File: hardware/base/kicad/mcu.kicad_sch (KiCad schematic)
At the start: 37 parts, among them J2 USB micro-B, J5 TC2030, SW1 BOOT, U2 TPD4E05U06DQAR, U9 STM32H523VET6

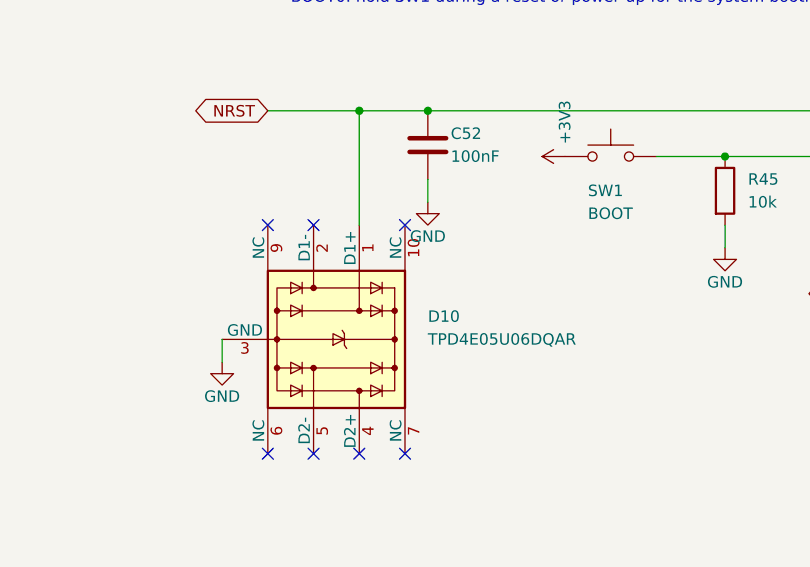
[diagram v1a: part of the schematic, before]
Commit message: Flow-through ESD arrays: the NC pin opposite each protected line carries it on every TPD4E05, not only on the PHY lines
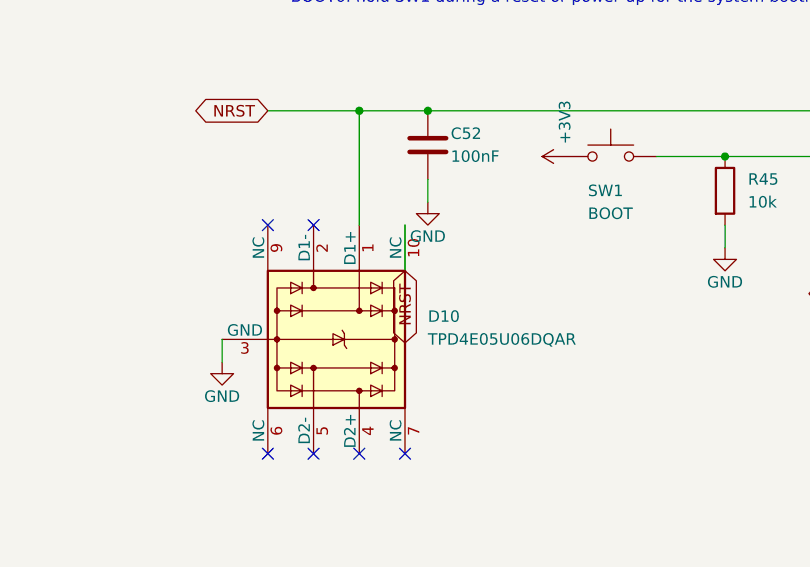
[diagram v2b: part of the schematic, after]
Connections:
- net NRST: now also D10.10 (NC)
- no-connect marks 10 -> 9

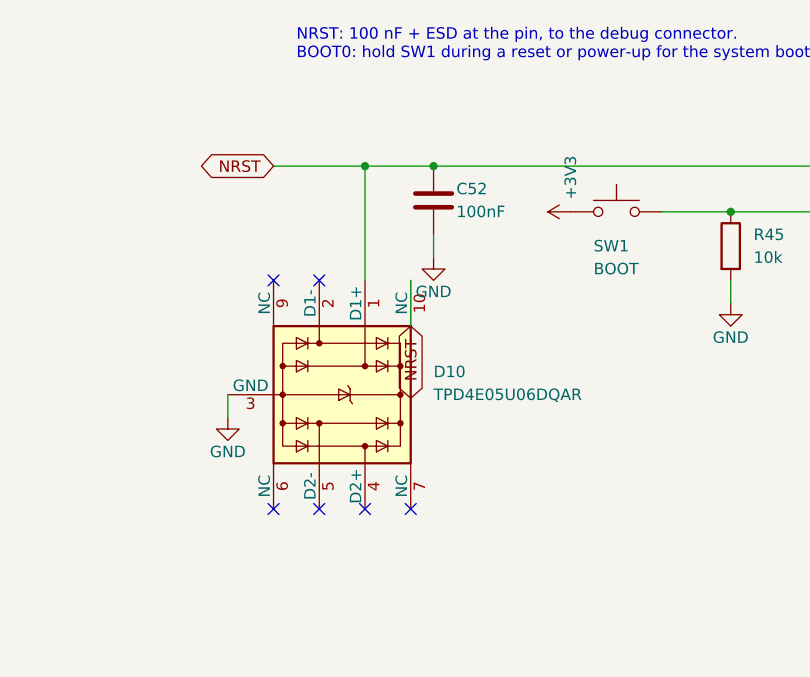
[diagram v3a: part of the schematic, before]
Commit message: Modbus termination always fitted (R246, removed for a master in the middle of the line); no ESD array on NRST; Ethernet line nets named TXA_P/TXA_N so that tools pair them
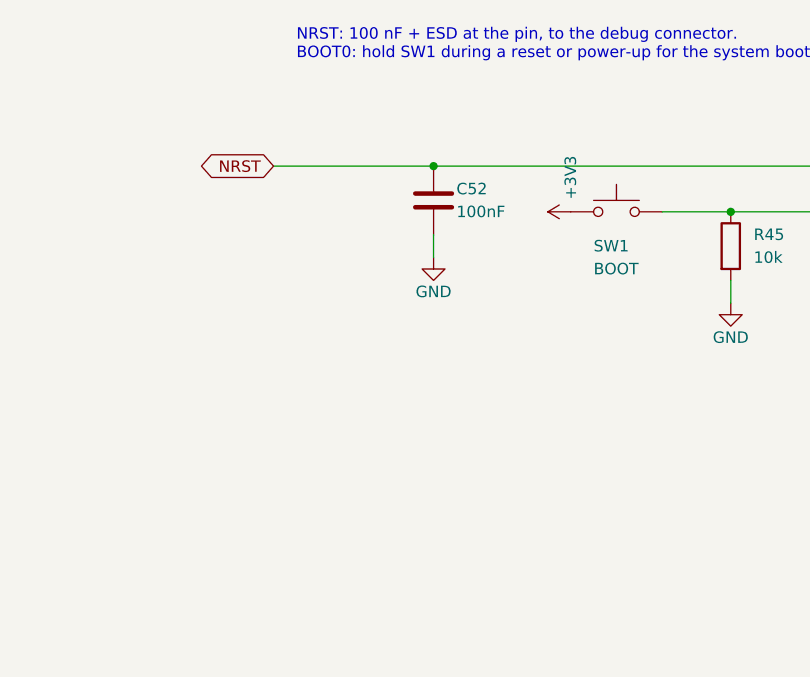
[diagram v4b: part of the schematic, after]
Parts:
- removed D10: TPD4E05U06DQAR, Package_SON:USON-10_2.5x1.0mm_P0.5mm, symbol Power_Protection:TPD4E05U06DQA
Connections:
- no-connect marks 9 -> 3

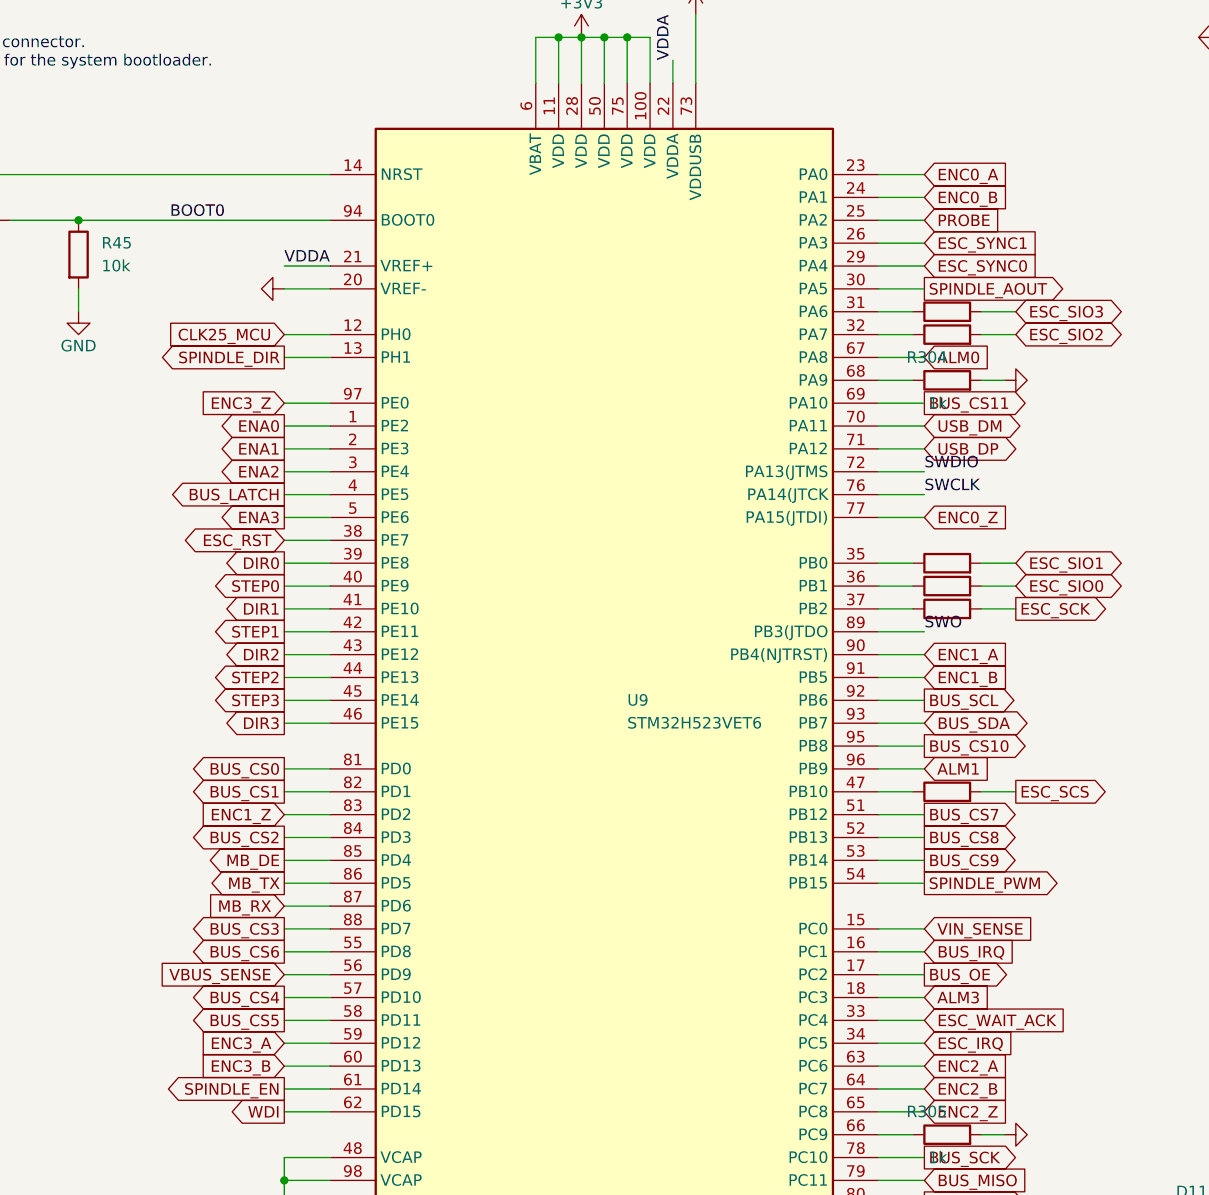
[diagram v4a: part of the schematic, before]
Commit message: Base: pin swaps of the placed board (chip selects, step/dir/enable channels, encoder timers 0 and 1, ribbon and Ethernet A ESD channels)
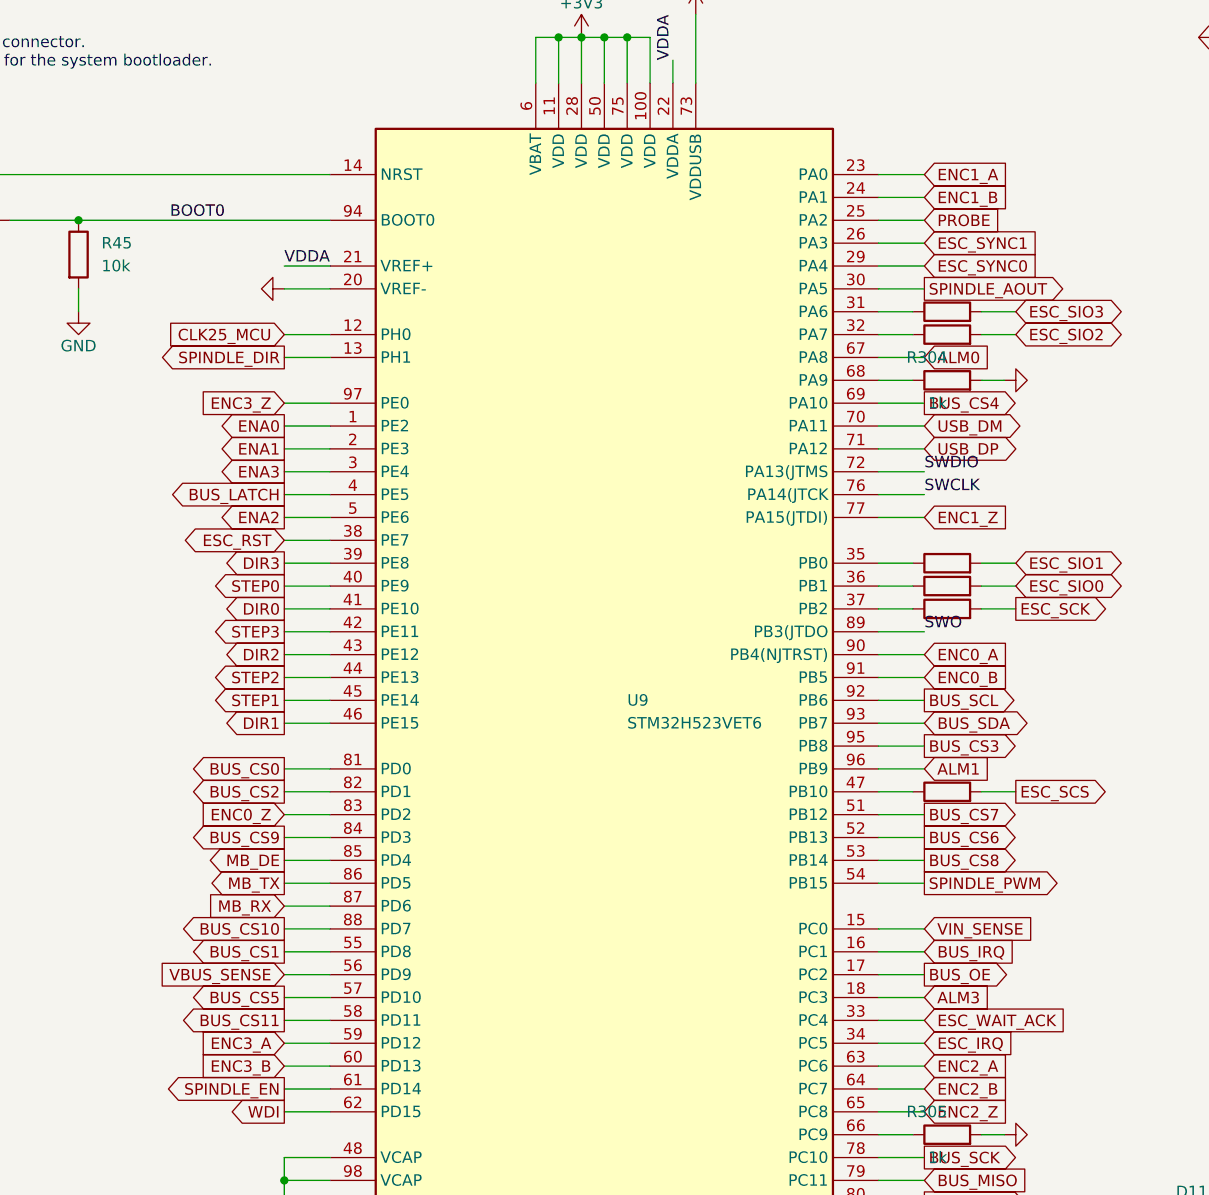
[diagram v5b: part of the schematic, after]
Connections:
- net BUS_CS1: now also U9.55 (PD8); no longer U9.82 (PD1)
- net BUS_CS10: now also U9.88 (PD7); no longer U9.95 (PB8)
- net BUS_CS11: now also U9.58 (PD11); no longer U9.69 (PA10)
- net BUS_CS2: now also U9.82 (PD1); no longer U9.84 (PD3)
- net BUS_CS3: now also U9.95 (PB8); no longer U9.88 (PD7)
- net BUS_CS4: now also U9.69 (PA10); no longer U9.57 (PD10)
- net BUS_CS5: now also U9.57 (PD10); no longer U9.58 (PD11)
- net BUS_CS6: now also U9.52 (PB13); no longer U9.55 (PD8)
- net BUS_CS8: now also U9.53 (PB14); no longer U9.52 (PB13)
- net BUS_CS9: now also U9.84 (PD3); no longer U9.53 (PB14)
- net DIR0: now also U9.41 (PE10); no longer U9.39 (PE8)
- net DIR1: now also U9.46 (PE15); no longer U9.41 (PE10)
- net DIR3: now also U9.39 (PE8); no longer U9.46 (PE15)
- net ENA2: now also U9.5 (PE6); no longer U9.3 (PE4)
- net ENA3: now also U9.3 (PE4); no longer U9.5 (PE6)
- net ENC0_A: now also U9.90 (PB4(NJTRST)); no longer U9.23 (PA0)
- net ENC0_B: now also U9.91 (PB5); no longer U9.24 (PA1)
- net ENC0_Z: now also U9.83 (PD2); no longer U9.77 (PA15(JTDI))
- net ENC1_A: now also U9.23 (PA0); no longer U9.90 (PB4(NJTRST))
- net ENC1_B: now also U9.24 (PA1); no longer U9.91 (PB5)
- net ENC1_Z: now also U9.77 (PA15(JTDI)); no longer U9.83 (PD2)
- net STEP1: now also U9.45 (PE14); no longer U9.42 (PE11)
- net STEP3: now also U9.42 (PE11); no longer U9.45 (PE14)

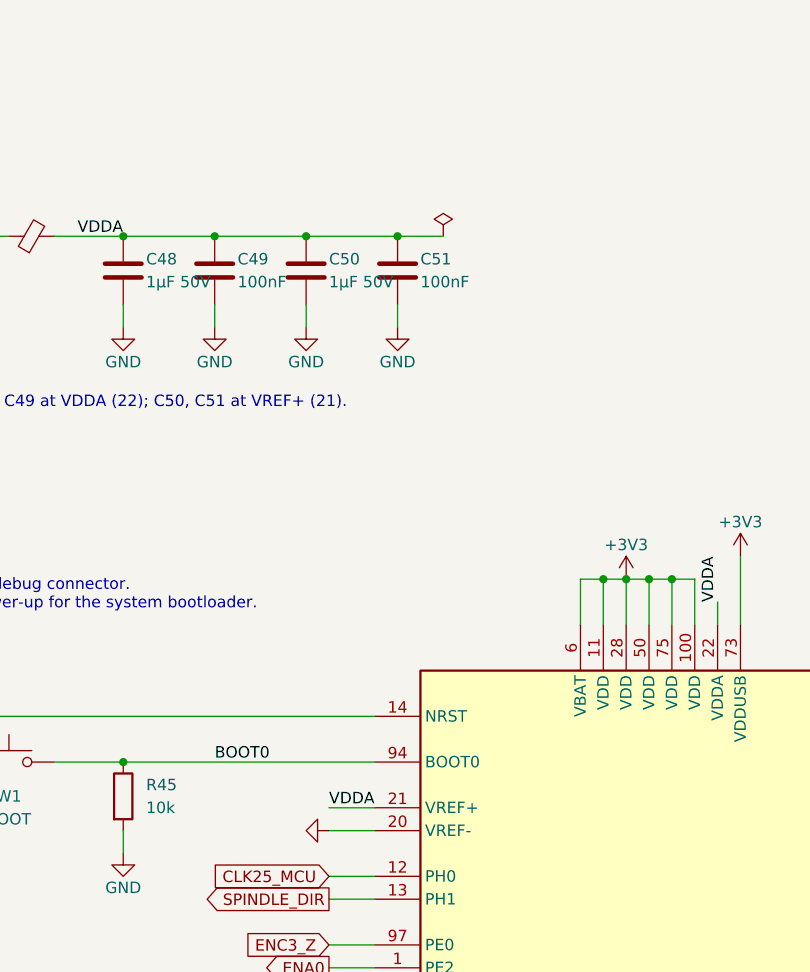
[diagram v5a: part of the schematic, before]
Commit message: Base: VREF+ filtered from VDDA through 49.9 ohm (R316, AN5711 47 ohm option)
VREF+ (pin 21) was tied straight to VDDA. It now has its own net, fed from
VDDA through R316 (49.9 ohm, palette value) and decoupled by C50 and C51:
with C50 (1 uF) the filter corner is 3.2 kHz. ERC 0, netlist 0.
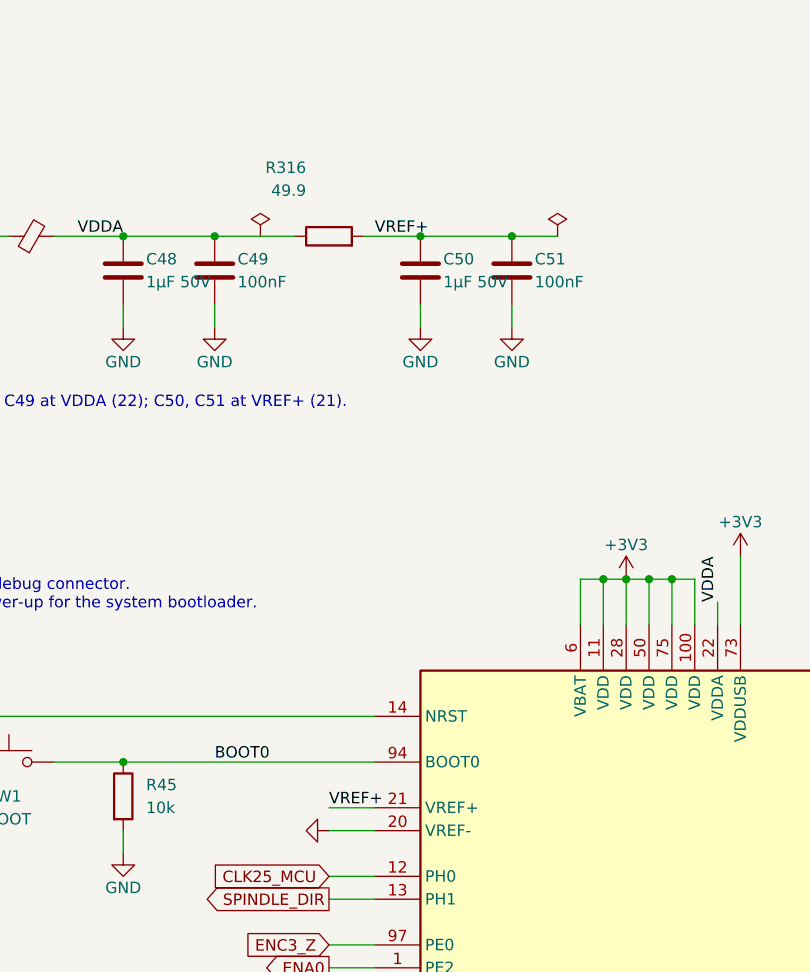
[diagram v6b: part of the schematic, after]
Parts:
- added R316: 49.9, Resistor_SMD:R_0603_1608Metric, symbol Device:R
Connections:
- net VDDA: now also R316.1; no longer C50.1, C51.1, U9.21 (VREF+)
- new net VREF+: C50.1, C51.1, R316.2, U9.21 (VREF+)
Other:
- moved on the sheet: C50, C51
